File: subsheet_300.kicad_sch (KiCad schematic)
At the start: 5 parts, among them U300_DIP40 ST_DMA_DIP40_PHY, U300_PLCC44 ST_DMA_PLCC44_PHY

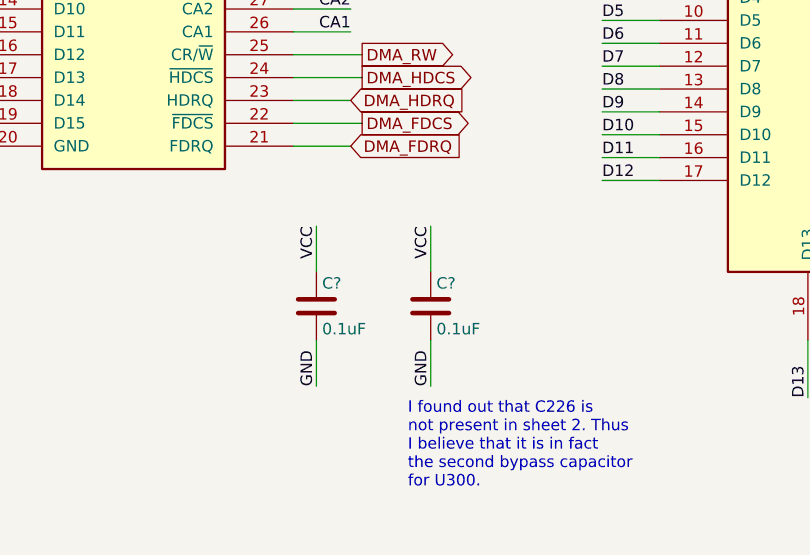
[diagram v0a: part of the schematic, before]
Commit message: Resolves #3 : [schematic] annotate video port with signal name
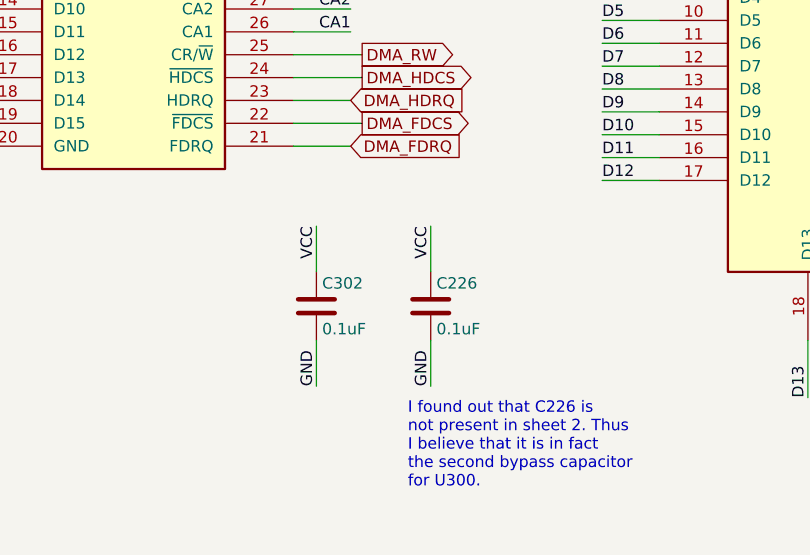
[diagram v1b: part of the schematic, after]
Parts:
- gave numbers to parts that had none: 2
